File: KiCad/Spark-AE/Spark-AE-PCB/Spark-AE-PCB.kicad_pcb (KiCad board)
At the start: 2 copper layers, 50 x 100 mm, 167 parts, among them CN1 I2C_IN, CN2 I2C_OUT, J1 Conn_01x20_Socket, J2 Conn_01x20_Socket, J3 AE_BUS, J4 Inputs, J5 Outputs, J6 Conn_02x06_Top_Bottom, Q1 AO3401, Q2 2N3904, Q3 2N3904, SW1 SW_Push, SW2 SW_Push, U2 MCP6002T-I_MS, U3 Driver_LED_PCA9633PW,118, U4 MCP6002T-I_MS, U5 MCP6002T-I_MS, U6 MCP6002T-I_MS, U7 Connector_Micro_SD_Card_Yamai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, U8 MCP6002T-I_MS, U9 74xGxx_MDD_74AHCT1G125GV

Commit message: pcb layout complete. ready for final pre-fab confirmation.
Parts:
- removed C31, C56: 10uF, Capacitor_SMD:C_0603_1608Metric
- removed C32, C55: 100nF, Capacitor_SMD:C_0603_1608Metric
- removed the C49 at (65.4, 80.0)
- removed the C50 at (65.4, 82.5)
- removed F2: nSMD050-33V, Fuse:Fuse_0603_1608Metric
- removed the R51 at (95.3, 76.9)
- removed the R55 at (171.3, 68.9)
- removed the R56 at (171.3, 71.4)
- removed R57, R58, R59: 47K, Resistor_SMD:R_0603_1608Metric
- removed U7: Connector_Micro_SD_Card_Yamaichi_PJS008U-3000-0, clectric-diy:PJS008U-3000-0
- added C39: 100nF, Capacitor_SMD:C_0603_1608Metric, F.Cu at (109.2, 143.3)
- added C40: 10uF, Capacitor_SMD:C_0603_1608Metric, F.Cu at (107.6, 143.3)
- added F1: nSMD050-33V, Fuse:Fuse_0603_1608Metric, F.Cu at (110.7, 143.3)
- added J7: SD_CONN, Connector_PinSocket_2.54mm:PinSocket_2x04_P2.54mm_Vertical, F.Cu at (83.4, 112.1)
- added R50: 1K, Resistor_SMD:R_0603_1608Metric, F.Cu at (121.0, 50.3)
- added R52: 1K, Resistor_SMD:R_0603_1608Metric, F.Cu at (121.0, 55.4)
- added R53: 100K, Resistor_SMD:R_0603_1608Metric, F.Cu at (95.1, 73.6)
- C49: renamed from C51; moved to F.Cu
- C50: renamed from C52; moved to F.Cu
- CN1, CN2: moved to B.Cu
- J6: value Conn_02x06_Top_Bottom -> SPI
- R76: renamed from R74; moved to F.Cu
- R77: renamed from R75; moved to F.Cu
- moved C12 79.9 mm to (103.7, 115.5), turned to 90 degrees
- moved C13 78.3 mm to (103.7, 121.5), turned to -90 degrees
- moved R26 76.7 mm to (109.1, 119.9), turned to -90 degrees
- moved R25 75.0 mm to (107.6, 118.2), turned to 90 degrees
- moved R21 69.3 mm to (117.9, 117.9)
- moved R80 68.3 mm to (85.6, 88.7), turned to -90 degrees
- moved R15 66.6 mm to (117.9, 116.3)
- moved R81 63.6 mm to (85.4, 96.7), turned to -90 degrees
- moved R82 63.2 mm to (85.4, 99.7), turned to -90 degrees
- moved R79 63.0 mm to (82.7, 90.7), turned to -90 degrees
- moved R78 59.0 mm to (80.4, 91.4)
- moved R5 58.8 mm to (117.9, 102.6)
- moved R31 58.0 mm to (86.7, 122.4), turned to -90 degrees
- moved C14 57.7 mm to (79.6, 124.0), turned to 90 degrees
- moved R2 56.3 mm to (117.9, 101.1)
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- renumbered C44 to C43, C47 to C44, C48 to C45, C45 to C46, C43 to C47, C46 to C48, C53 to C51, C54 to C52, R50 to R51, R52 to R54, R53 to R55, R54 to R56, R60 to R62, R61 to R63, R62 to R64, R63 to R65, R64 to R66, R65 to R67, R66 to R68, R67 to R69, R68 to R70, R69 to R71, R71 to R72, R72 to R73, R73 to R74, R70 to R75, R76 to R78, R77 to R79, R78 to R80, R79 to R81, R80 to R82
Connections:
- net I2C_IN_SCL renamed I2C_SCL_BUS
- net I2C_IN_SDA renamed I2C_SDA_BUS
- C49 pad 1: +3.3V -> GND
- C49 pad 2: GND -> +3.3V
- C50 pad 1: +3.3V -> GND
- C50 pad 2: GND -> +3.3V
- CN1 pad 1: +3.3V -> GND
- CN1 pad 2: GND -> +3.3V
- CN2 pad 1: +3.3V -> GND
- CN2 pad 2: GND -> +3.3V
- R30 pad 1: Net-(D3-Pad4) -> ENC_LED_BLUE
- R30 pad 2: ENC_LED_BLUE -> Net-(D3-Pad4)
- R62 pad 1: VREF_1V65 -> Net-(R62-Pad1)
- R62 pad 2: Net-(R60-Pad2) -> VREF_1V65
- U6 pad 7: Net-(R60-Pad2) -> Net-(R62-Pad1)
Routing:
- net +3.3V: track 111.5 -> 261.8 mm, vias 2 -> 8
- net D0_AE_OUT: track 5.29 -> 99.5 mm, vias 0 -> 6
- net SW2_CV: track 2.26 -> 87.8 mm, vias 0 -> 4
- net Net-(Q3-B): track 90.6 -> 9.29 mm, vias 2 -> 0
- net I2C_SDA: track 6.87 -> 80.2 mm, vias 0 -> 2
- net SW1_CV: track 2.42 -> 74.6 mm, vias 0 -> 4
- net I2C_SCL: track 6.02 -> 78.0 mm, vias 0 -> 2
- net Net-(Q2-B): track 78.5 -> 9.74 mm, vias 2 -> 0
- net Net-(U4B--): track 63.9 -> 4.98 mm
- net AUDIO_IN_2: track 7.96 -> 63.7 mm
- net Net-(U4A--): track 55.7 -> 2.02 mm
- net AUDIO_IN_1: track 2.50 -> 53.6 mm
- net GND: track 49.5 -> 94.8 mm, vias 45 -> 69
- net +5V: track 203.7 -> 247.2 mm
- net Net-(C23-Pad1): track 33.9 -> 3.07 mm, vias 2 -> 0
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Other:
- board text added: "-RED-"
- board text added: "Copyright © 2026 clectric.diy Licensed under CERN-OHL-S v2"

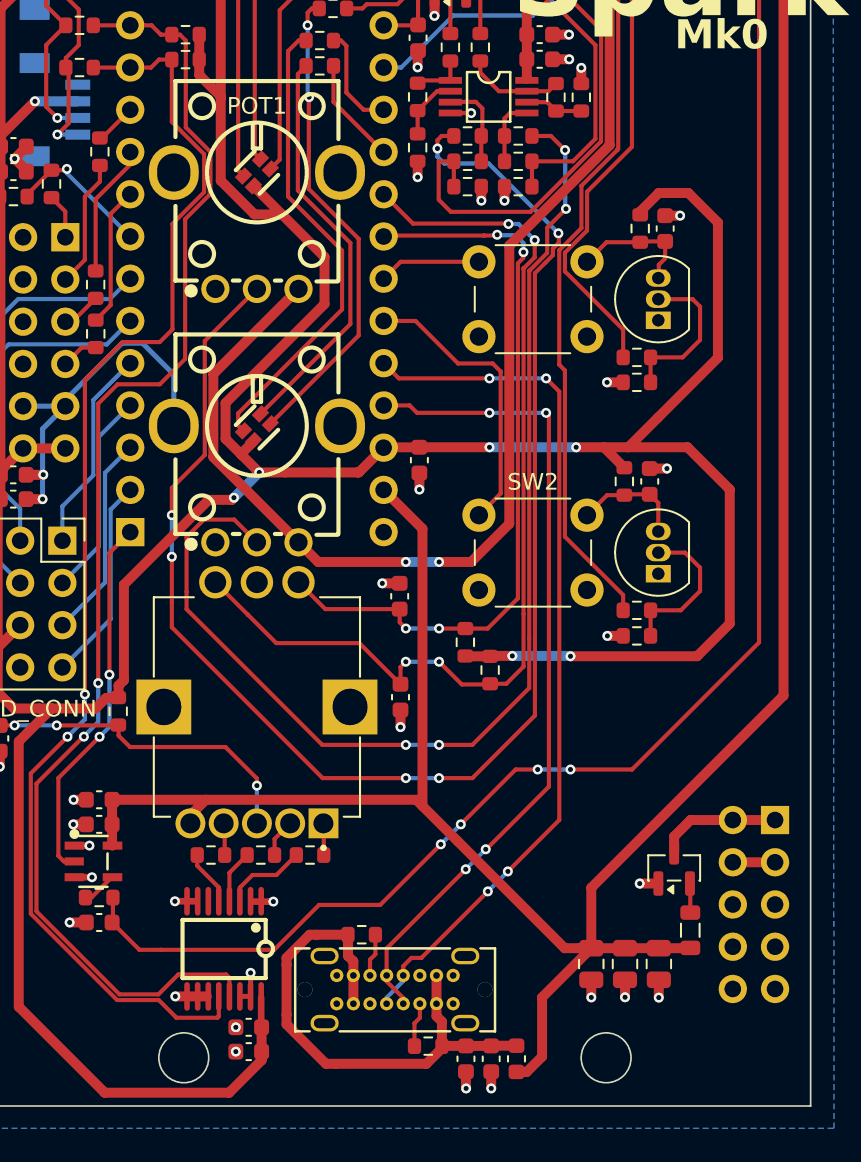
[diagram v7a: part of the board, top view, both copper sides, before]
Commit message: mk0 prototype sent for production! commit includes a couple of necessary tweaks.
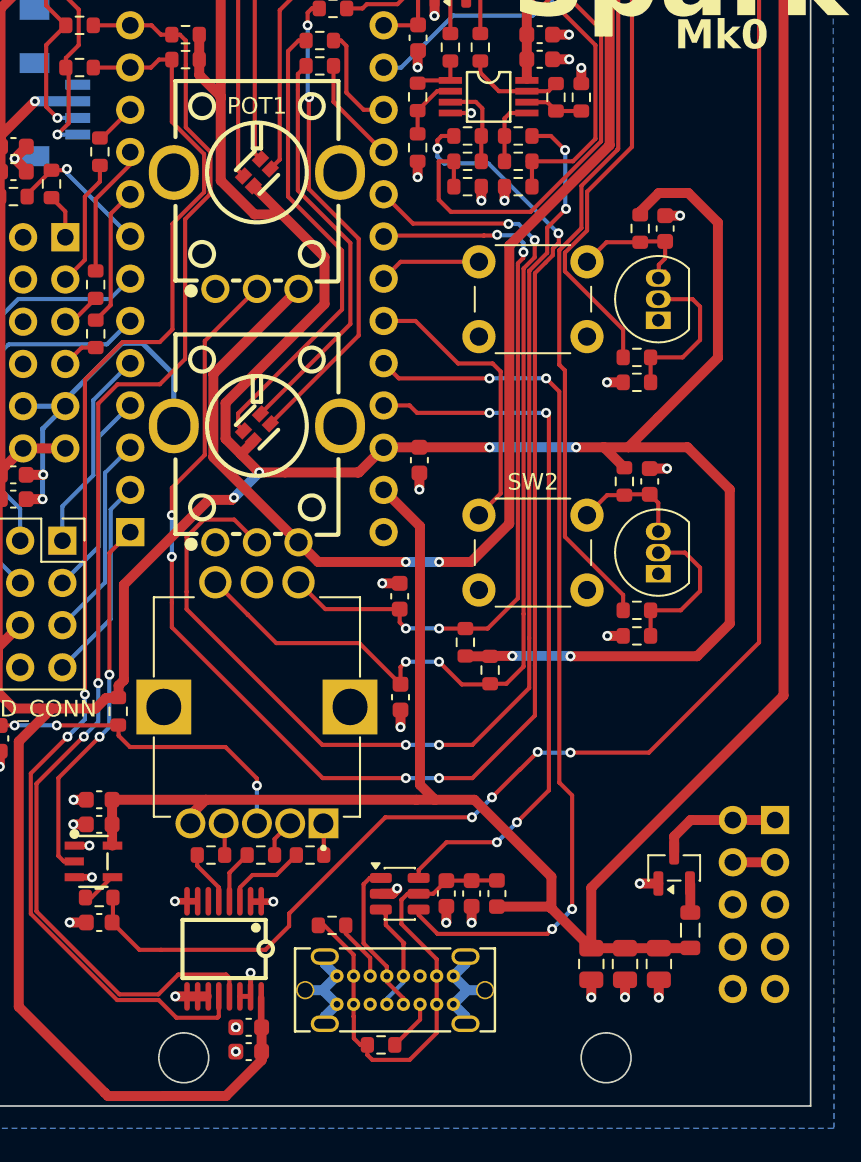
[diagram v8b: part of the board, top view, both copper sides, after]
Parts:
- added G***: LOGO, clectric-branding:clectric.diy-Wordmark-20mm, B.Cu at (114.5, 122.2)
- added U7: USBLC6-2SC6, Package_TO_SOT_SMD:SOT-23-6, F.Cu at (103.7, 133.4)
- F1: value nSMD050-33V -> SMD0603-050
- FB1: value FerriteBead -> GZ2012D560TF
- moved C40 10.0 mm to (106.5, 133.4)
- moved C39 10.0 mm to (108.0, 133.4)
- moved F1 10.0 mm to (109.5, 133.4)
- moved R67 9.28 mm to (99.6, 135.3), turned to 0 degrees
- moved R64 6.73 mm to (102.5, 142.5)
- turned USB1 to 180 degrees
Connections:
- USB1 pad A6: USB_D+ -> Net-(U7-I/O1-Pad1)
- USB1 pad A7: USB_D- -> Net-(U7-I/O2-Pad3)
- USB1 pad B6: USB_D+ -> Net-(U7-I/O1-Pad1)
- USB1 pad B7: USB_D- -> Net-(U7-I/O2-Pad3)
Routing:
- net GND: track 94.8 -> 108.6 mm, vias 69 -> 70
- net Net-(U7-I/O1-Pad1): track 0.00 -> 9.41 mm
- net USB_D+: track 50.8 -> 43.7 mm
- net Net-(U7-I/O2-Pad3): track 0.00 -> 6.71 mm
- net +5V: track 247.2 -> 241.2 mm
- net Net-(U7-VBUS): track 32.3 -> 29.5 mm
- net Net-(USB1-CC2): track 2.68 -> 3.66 mm
- net USB_D-: track 52.7 -> 53.4 mm
